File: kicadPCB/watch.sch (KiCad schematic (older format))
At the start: 62 parts, among them IC1 ISL1209, J2 USB-MICROB, M1 BOS_LIBS_SWD_BREAKOUTS, T1 BC850, U2 MKL27Z256VLH4, Y1 Crystal

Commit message: fixed spi1
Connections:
- net PTB16: now also U$4.DS
- net PTB19: no longer U$4.DS
- net PTC0: no longer U$4.SHCP, U$5.SHCP
- net PTC3: now reaches U2.46 (PTC3/LLWU_P7)
- net PTC3: now also U$4.SHCP, U$5.SHCP
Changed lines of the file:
@@
 PTB17
 Text Label 7950 5450 0    65   ~ 0
-PTB19
+PTB16
 Text Label 9050 3950 1    65   ~ 0
-PTC0
+PTC3
 Text Label 9250 3950 0    65   ~ 0
 PTC2
@@
 Text Label 14350 10350 0    10   ~ 0
 PTB18
-Text Label 8650 5450 2    10   ~ 0
-PTB19
 Text Label 14350 10250 0    10   ~ 0
 PTB19
 Text Label 14350 10150 0    10   ~ 0
-PTC0
-Text Label 9050 4350 1    10   ~ 0
-PTC0
-Text Label 11650 6350 2    10   ~ 0
 PTC0
 Text Label 14350 9950 0    10   ~ 0
@@
 	0    -1   -1   0
 $EndComp
+Wire Wire Line
+	14350 9850 14600 9850
+Text Label 14600 9850 0    60   ~ 0
+PTC3
 $EndSCHEMATC

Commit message: fixed resistor vals
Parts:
- R10, R3, R4, R5, R6, R7, R8, R9: value 680 -> 330
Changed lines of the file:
@@
 P 11350 3150
 F 0 "R3" H 11200 3208 70  0000 L BNN
-F 1 "680" H 11201 3020 70  0000 L BNN
+F 1 "330" H 11201 3020 70  0000 L BNN
 F 2 "watch:SPARKFUN-RESISTORS_0603-RES" H 11340 2940 65  0001 L TNN
 F 3 "" H 11350 3150 60  0001 C CNN
@@
 P 11650 3150
 F 0 "R4" H 11500 3208 70  0000 L BNN
-F 1 "680" H 11501 3020 70  0000 L BNN
+F 1 "330" H 11501 3020 70  0000 L BNN
 F 2 "watch:SPARKFUN-RESISTORS_0603-RES" H 11640 2940 65  0001 L TNN
 F 3 "" H 11650 3150 60  0001 C CNN
@@
 P 11450 3550
 F 0 "R5" H 11300 3608 70  0000 L BNN
-F 1 "680" H 11301 3420 70  0000 L BNN
+F 1 "330" H 11301 3420 70  0000 L BNN
 F 2 "watch:SPARKFUN-RESISTORS_0603-RES" H 11440 3340 65  0001 L TNN
 F 3 "" H 11450 3550 60  0001 C CNN
@@
 P 11550 2750
 F 0 "R6" H 11400 2808 70  0000 L BNN
-F 1 "680" H 11401 2620 70  0000 L BNN
+F 1 "330" H 11401 2620 70  0000 L BNN
 F 2 "watch:SPARKFUN-RESISTORS_0603-RES" H 11540 2540 65  0001 L TNN
 F 3 "" H 11550 2750 60  0001 C CNN
@@
 P 14150 2750
 F 0 "R7" H 14000 2808 70  0000 L BNN
-F 1 "680" H 14001 2620 70  0000 L BNN
+F 1 "330" H 14001 2620 70  0000 L BNN
 F 2 "watch:SPARKFUN-RESISTORS_0603-RES" H 14140 2540 65  0001 L TNN
 F 3 "" H 14150 2750 60  0001 C CNN
@@
 P 14250 3350
 F 0 "R8" H 14100 3408 70  0000 L BNN
-F 1 "680" H 14101 3220 70  0000 L BNN
+F 1 "330" H 14101 3220 70  0000 L BNN
 F 2 "watch:SPARKFUN-RESISTORS_0603-RES" H 14240 3140 65  0001 L TNN
 F 3 "" H 14250 3350 60  0001 C CNN
@@
 P 14350 3850
 F 0 "R9" H 14200 3908 70  0000 L BNN
-F 1 "680" H 14201 3720 70  0000 L BNN
+F 1 "330" H 14201 3720 70  0000 L BNN
 F 2 "watch:SPARKFUN-RESISTORS_0603-RES" H 14340 3640 65  0001 L TNN
 F 3 "" H 14350 3850 60  0001 C CNN
@@
 P 14450 4250
 F 0 "R10" H 14300 4308 70  0000 L BNN
-F 1 "680" H 14301 4120 70  0000 L BNN
+F 1 "330" H 14301 4120 70  0000 L BNN
 F 2 "watch:SPARKFUN-RESISTORS_0603-RES" H 14440 4040 65  0001 L TNN
 F 3 "" H 14450 4250 60  0001 C CNN
@@
 Text Label 14350 10550 0    10   ~ 0
 PTB16
-Text Label 9350 6450 3    10   ~ 0
-PTB17
-Text Label 13750 6050 0    10   ~ 0
-PTB17
 Text Label 14350 10450 0    10   ~ 0
 PTB17
@@
 Text Label 14350 9950 0    10   ~ 0
 PTC2
-Text Label 9250 4350 1    10   ~ 0
-PTC2
 Text Label 14350 9550 0    10   ~ 0

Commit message: fixed uart gps
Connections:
- net PTC11: no longer GPTX46.2
- net PTD2: now also GPTX46.2; no longer D3.2 (A)
- net PTE0: now also D3.2 (A)
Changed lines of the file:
@@
 PTC10
 Text Label 16150 11250 0    65   ~ 0
-PTC11
+PTD2
 Text Label 2250 12050 0    65   ~ 0
 PTD1
-Text Label 3950 13650 0    65   ~ 0
-PTD2
 Text Label 5850 12250 0    65   ~ 0
 PTD3
@@
 Text Label 14350 8850 0    10   ~ 0
 PTC11
-Text Label 16350 11250 2    10   ~ 0
-PTC11
 Text Label 14350 8650 0    10   ~ 0
 PTD1
@@
 PTD1
 Text Label 14350 8550 0    10   ~ 0
-PTD2
-Text Label 3950 13350 3    10   ~ 0
 PTD2
 Text Label 14350 8450 0    10   ~ 0
@@
 Text Label 14600 9850 0    60   ~ 0
 PTC3
+Text Label 3950 13650 0    60   ~ 0
+PTE0
 $EndSCHEMATC

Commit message: moved OE to a timer pin to control display brightness
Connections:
- net PTB17: no longer U$4.OE, U$5.OE
- net PTB18: now also U$4.OE, U$5.OE
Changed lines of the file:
@@
 PTA4
 Text Label 9750 6450 0    65   ~ 0
-PTB17
+PTB18
 Text Label 7950 5450 0    65   ~ 0
 PTB16

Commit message: wired storage clock together for SR
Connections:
- net PTC2: no longer U$4.STCP
- net PTC7: no longer U$5.STCP
- net PTD4: now reaches U2.61 (PTD4/LLWU_P14)
- net PTD4: now also U$4.STCP, U$5.STCP
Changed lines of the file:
@@
 PTC3
 Text Label 9250 3950 0    65   ~ 0
-PTC2
+PTD4
 Text Label 16250 9650 0    65   ~ 0
 PTC4
-Text Label 11350 6150 0    65   ~ 0
-PTC7
 Text Label 8350 11650 0    65   ~ 0
 PTC8
@@
 Text Label 14350 9250 0    10   ~ 0
 PTC7
-Text Label 11650 6150 2    10   ~ 0
-PTC7
 Text Label 14350 9150 0    10   ~ 0
 PTC8
 Text Label 15150 8950 3    10   ~ 0
-PTC8
-Text Label 8050 11650 0    10   ~ 0
 PTC8
 Text Label 8350 8450 0    10   ~ 0
@@
 PTC9
 Text Label 14750 8950 3    10   ~ 0
-PTC9
-Text Label 8050 11750 0    10   ~ 0
 PTC9
 Text Label 8350 8550 0    10   ~ 0
@@
 Connection ~ 14550 9250
 Wire Wire Line
-	11650 6150 11350 6150
+	11200 6150 11650 6150
 Wire Wire Line
 	14350 9150 15350 9150
@@
 Text Label 3950 13650 0    60   ~ 0
 PTE0
+Wire Wire Line
+	14350 8350 14500 8350
+Text Label 14500 8350 0    60   ~ 0
+PTD4
+Wire Wire Line
+	11200 6150 11200 4050
+Wire Wire Line
+	11200 4050 9250 4050
+Connection ~ 9250 4050
 $EndSCHEMATC

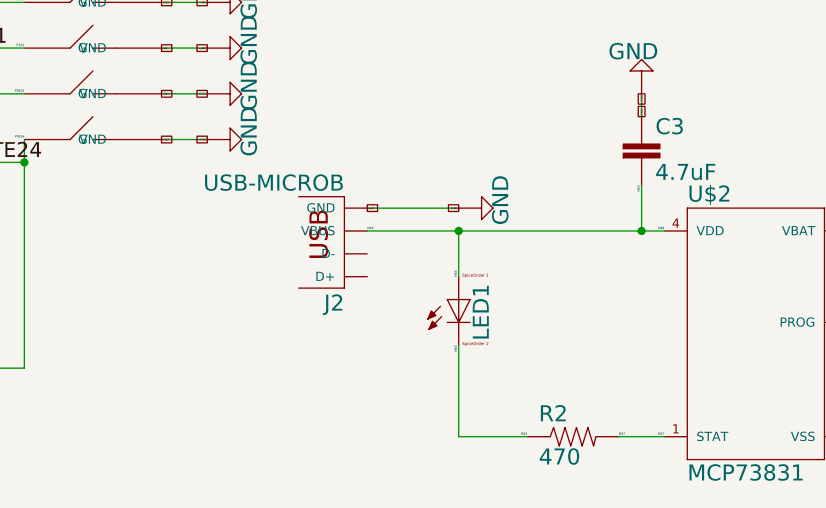
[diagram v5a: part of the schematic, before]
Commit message: added through hole usb
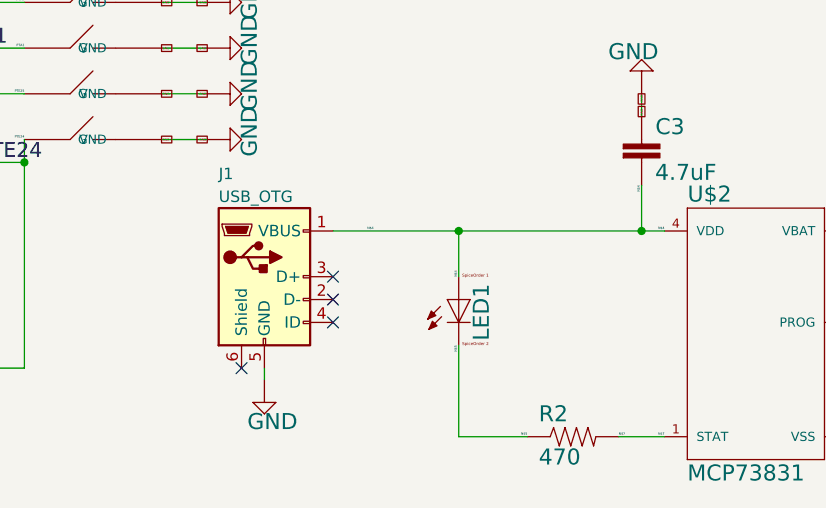
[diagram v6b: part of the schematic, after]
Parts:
- removed J2: USB-MICROB, watch:SPARKFUN-CONNECTORS_USB-MICROB, symbol SPARKFUN-CONNECTORS_USB
- added J1: USB_OTG, Connectors:USB_Micro-B, symbol USB_OTG
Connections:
- net GND: now also J1.5 (GND)
- net N$4: now also J1.1 (VBUS)
- no-connect marks 0 -> 4

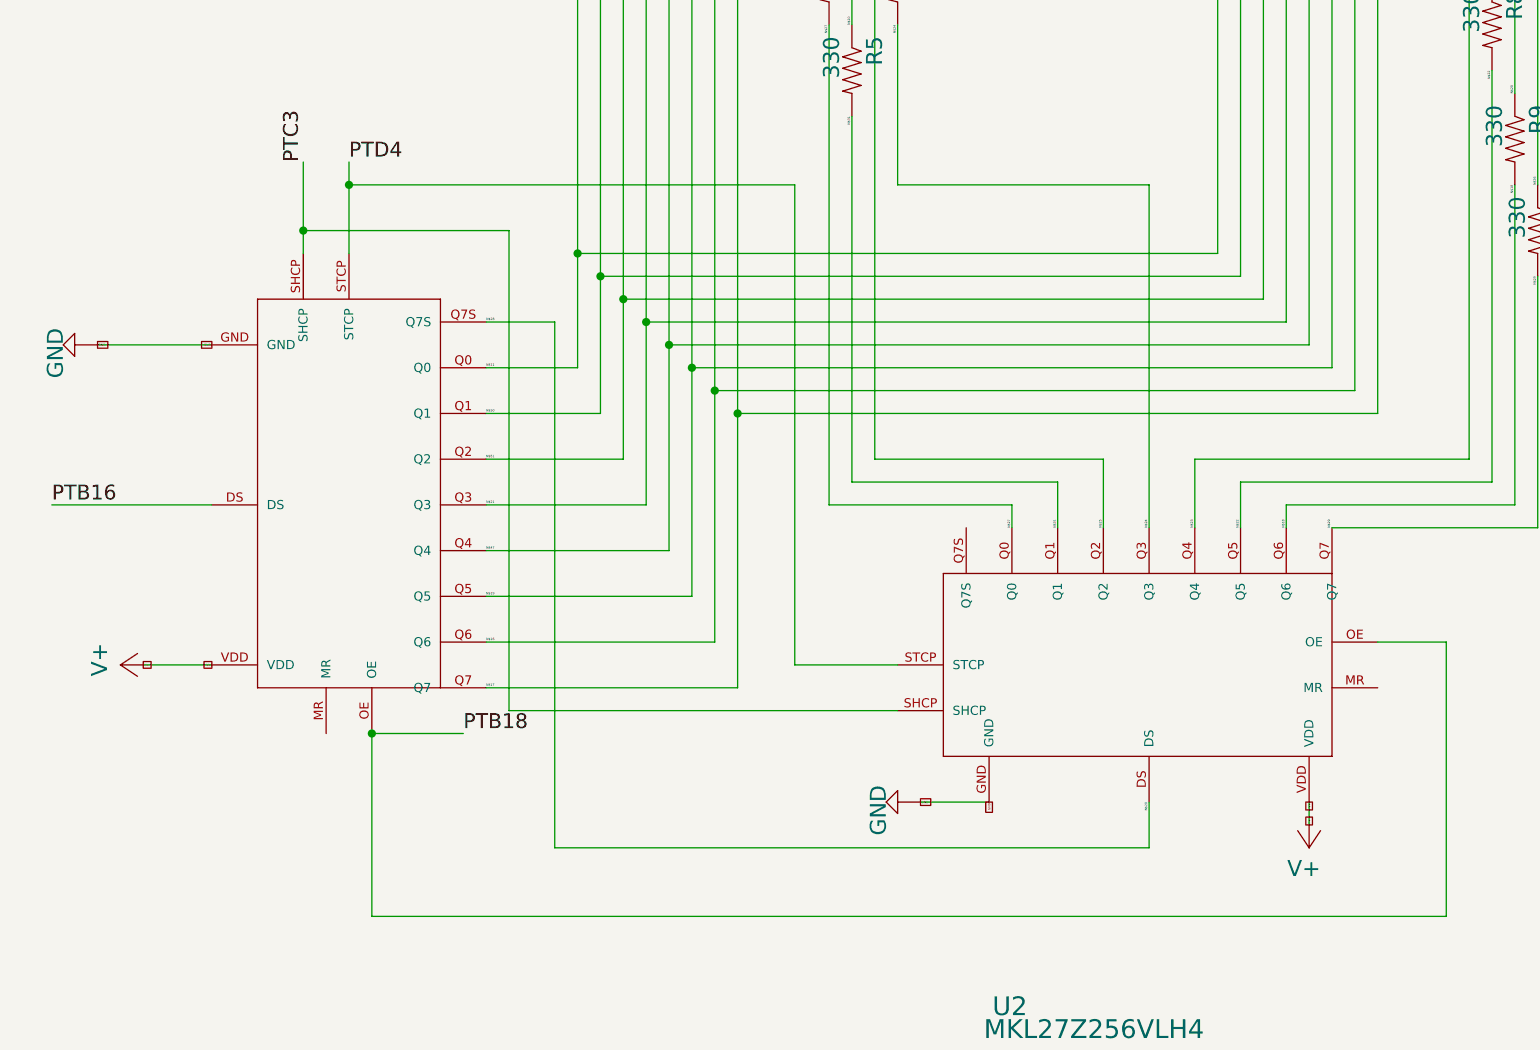
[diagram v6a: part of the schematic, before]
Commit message: fixed bad reset on SRs
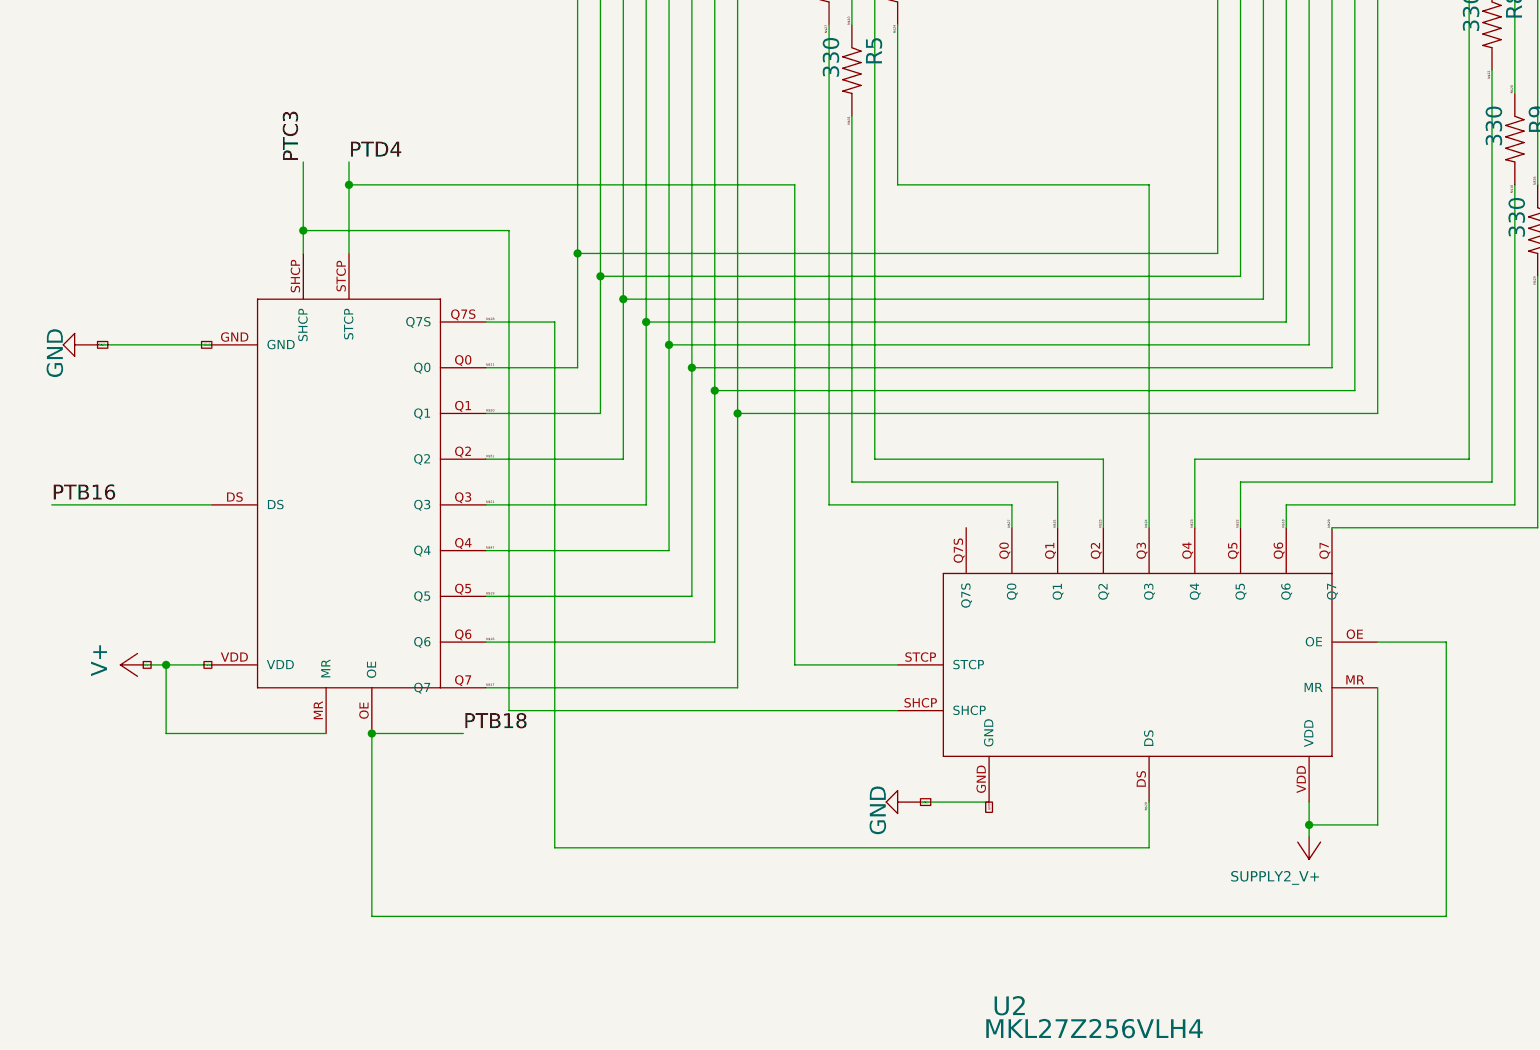
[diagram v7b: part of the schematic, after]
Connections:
- net V+: now also U$4.MR, U$5.MR
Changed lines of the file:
@@
-$EndComp
-$Comp
-L SUPPLY2_V+ #SUPPLY027
-U 1 1 58A21041
-P 13450 6950
-F 0 "#SUPPLY027" H 13400 7000 70  0001 L BNN
-F 1 "V+" H 13400 7000 70  0000 L BNN
-F 2 "" H 13450 6950 60  0001 C CNN
-F 3 "" H 13450 6950 60  0001 C CNN
-	1    13450 6950
-	-1   0    0    1
 $EndComp
 $Comp
@@
 Text GLabel 8650 6150 0    10   UnSpc ~ 0
 V+
-Text GLabel 13450 6750 3    10   UnSpc ~ 0
-V+
-Text GLabel 13450 6850 1    10   UnSpc ~ 0
-V+
 Text GLabel 6050 5850 1    10   UnSpc ~ 0
 V+
@@
 Connection ~ 14650 9950
 Wire Wire Line
-	9250 4350 9250 3950
+	9250 3950 9250 4350
 Wire Wire Line
 	14350 9550 14550 9550
@@
 Wire Wire Line
 	8350 6150 8650 6150
-Wire Wire Line
-	13450 6750 13450 6850
 Wire Wire Line
 	6050 5850 6050 5650
@@
 NoConn ~ 13100 13050
 NoConn ~ 13100 13150
+Wire Wire Line
+	9150 6450 8450 6450
+Wire Wire Line
+	8450 6450 8450 6150
+Connection ~ 8450 6150
+$Comp
+L SUPPLY2_V+ #SUPPLY?
+U 1 1 5A5F7150
+P 13450 7000
+F 0 "#SUPPLY?" H 13450 7000 45  0001 L BNN
+F 1 "SUPPLY2_V+" H 13400 7050 45  0000 L BNN
+F 2 "" H 13450 7000 60  0001 C CNN
+F 3 "" H 13450 7000 60  0001 C CNN
+	1    13450 7000
+	-1   0    0    1
+$EndComp
+Wire Wire Line
+	13450 6900 13450 6750
+Wire Wire Line
+	13750 6250 13750 6850
+Wire Wire Line
+	13750 6850 13450 6850
+Connection ~ 13450 6850
 $EndSCHEMATC

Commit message: fixed pnp
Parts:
- removed T2: ~, watch:TRANSISTOR_SOT23-EBC, symbol TRANSISTOR_-PNP-
- added Q1: Q_PNP_CEB, TO_SOT_Packages_SMD:SOT-23, symbol Q_PNP_BEC
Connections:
- net N$6: now also Q1.3 (C)
- net PTC4: now also Q1.1 (B)
- net V+: now also Q1.2 (E)
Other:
- moved on the sheet: C1
